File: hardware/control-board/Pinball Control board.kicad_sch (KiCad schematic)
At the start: 83 parts, among them J1 Connector C, J2 Conn_01x10_Pin, J3 B4B-XH-A, J4 Conn_01x10_Pin, SW1 test switch, SW2 test switch, U1 TPS1H200AQDGNRQ1, U2 TPS1H200AQDGNRQ1, U3 TPS1H200AQDGNRQ1, U4 TPS1H200AQDGNRQ1, U5 TPS1H200AQDGNRQ1

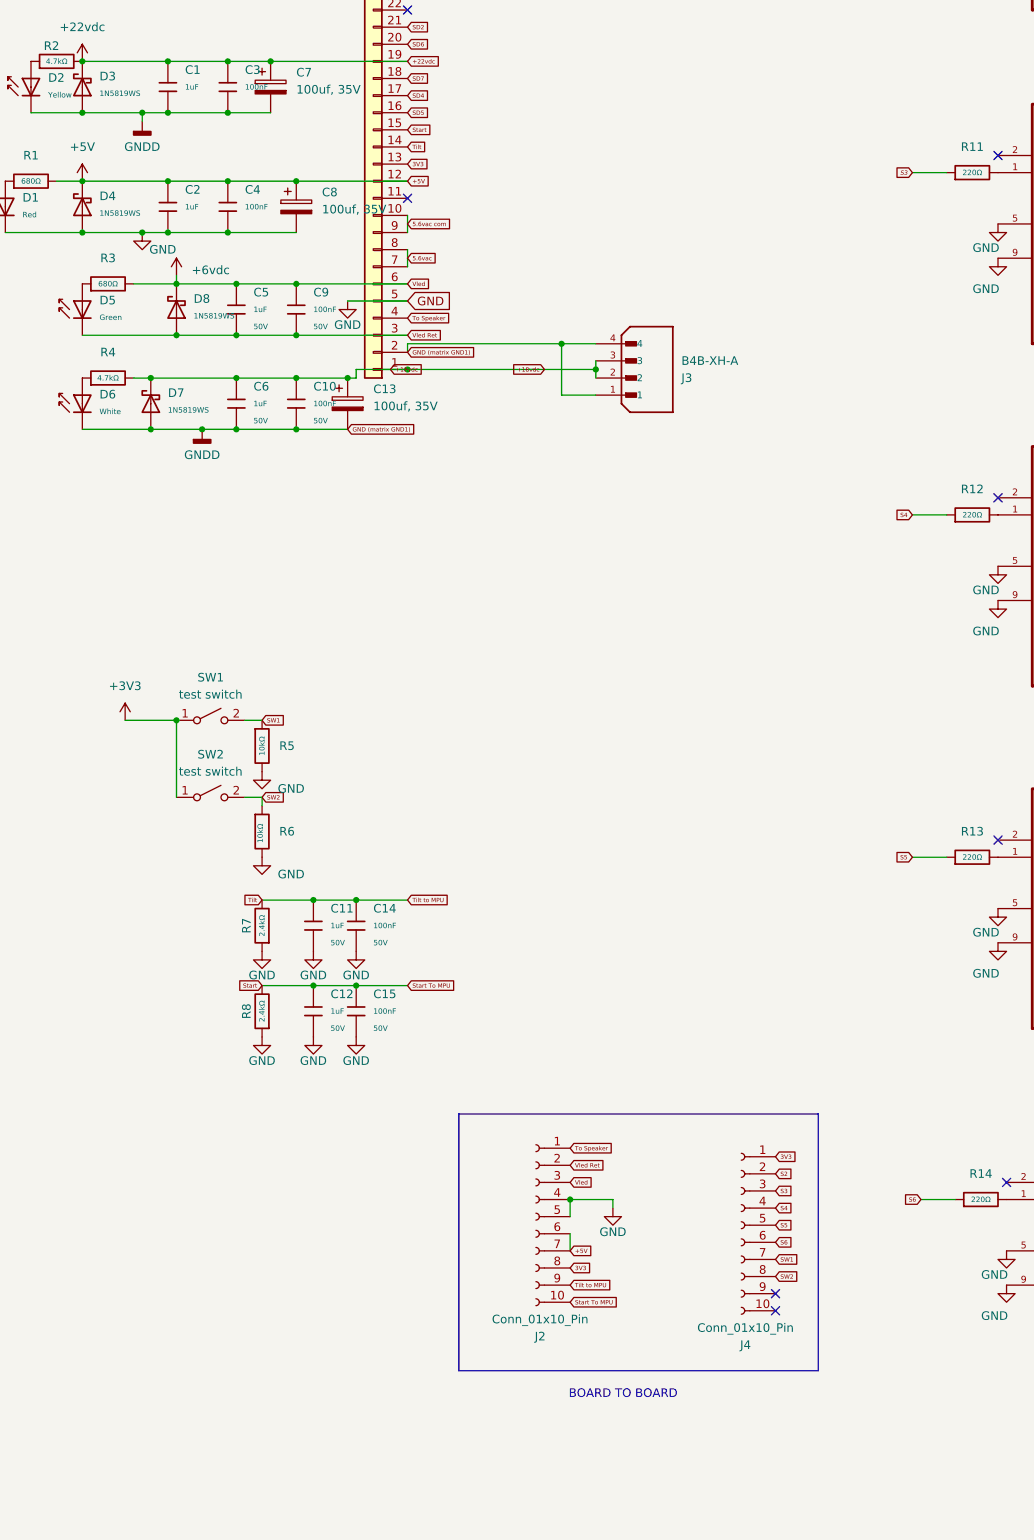
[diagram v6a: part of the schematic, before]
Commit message: Checkpoint KiCad schematic and PCB updates
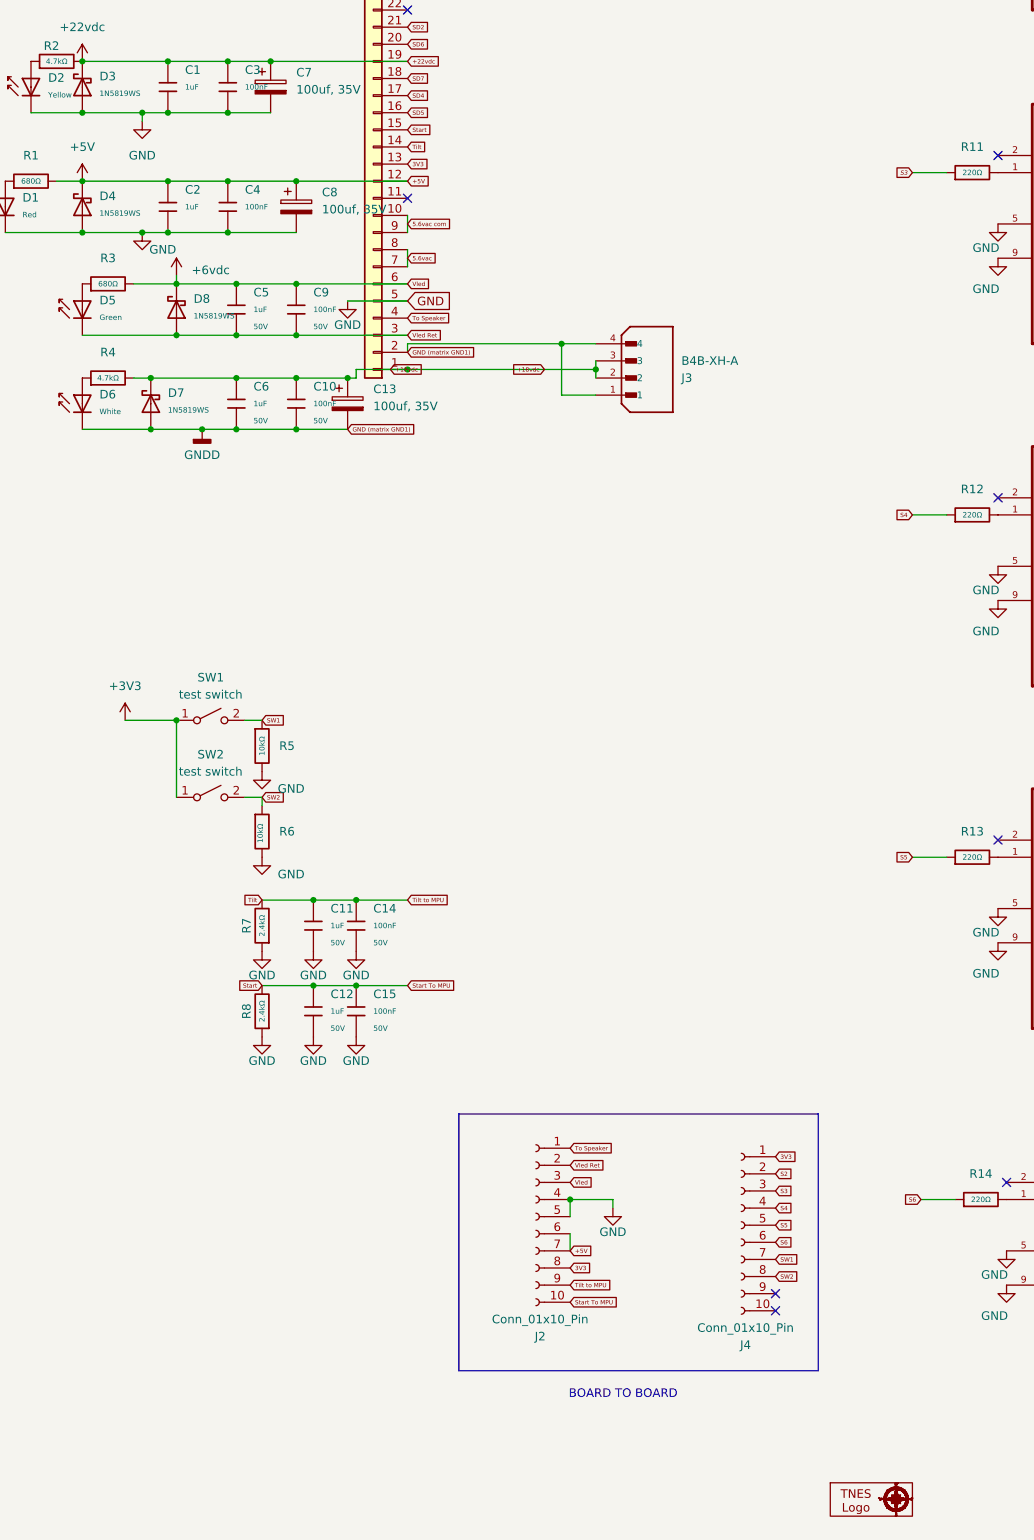
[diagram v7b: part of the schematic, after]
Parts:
- added 10mm1: ~, 1My_Parts_ Passive:10mm LOGO, symbol 1My_Passive:TNES_Logo_10mm
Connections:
- net GND: now also C1.2, C3.2, C7.2, D2.1, D3.2
- net GNDD: no longer C1.2, C3.2, C7.2, D2.1, D3.2
